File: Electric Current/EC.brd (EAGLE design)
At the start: 61.3 x 30.5 mm, 24 parts, among them IC1 LD117AS33TR

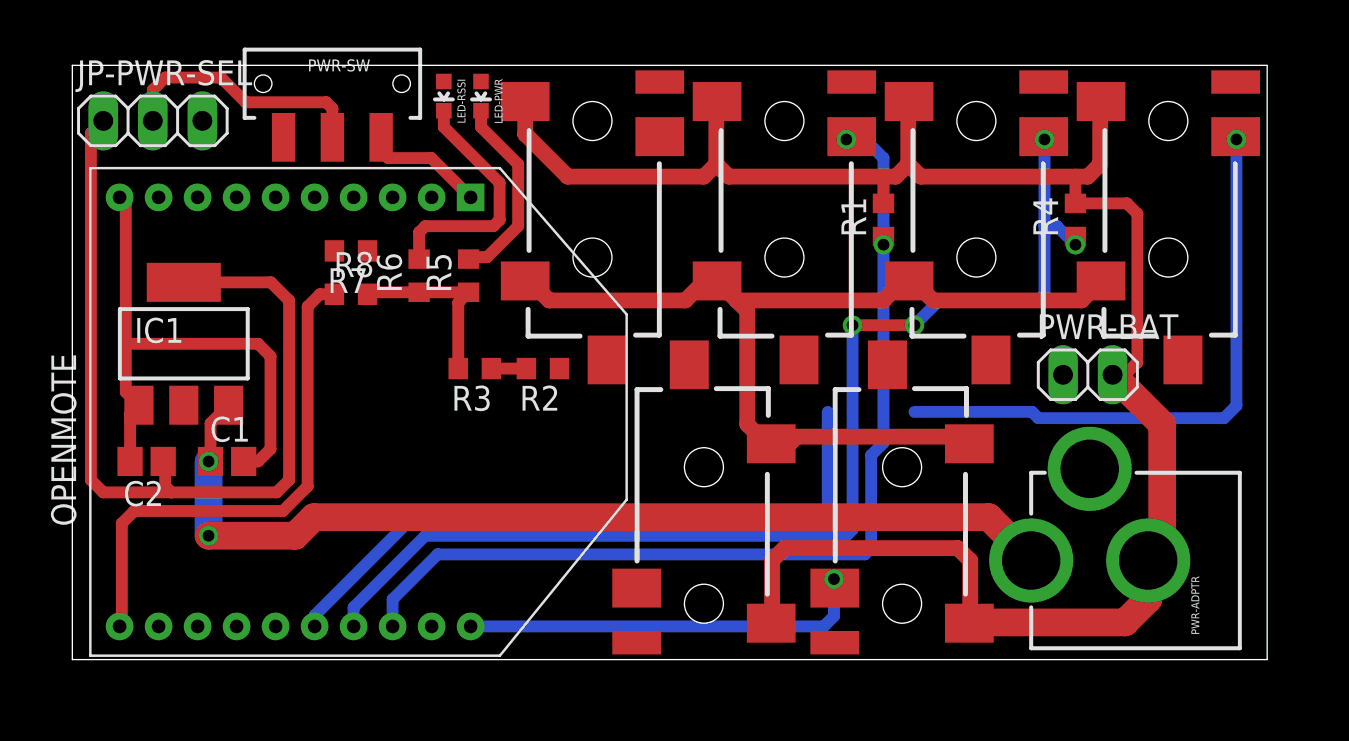
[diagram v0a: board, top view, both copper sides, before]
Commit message: Electric current module
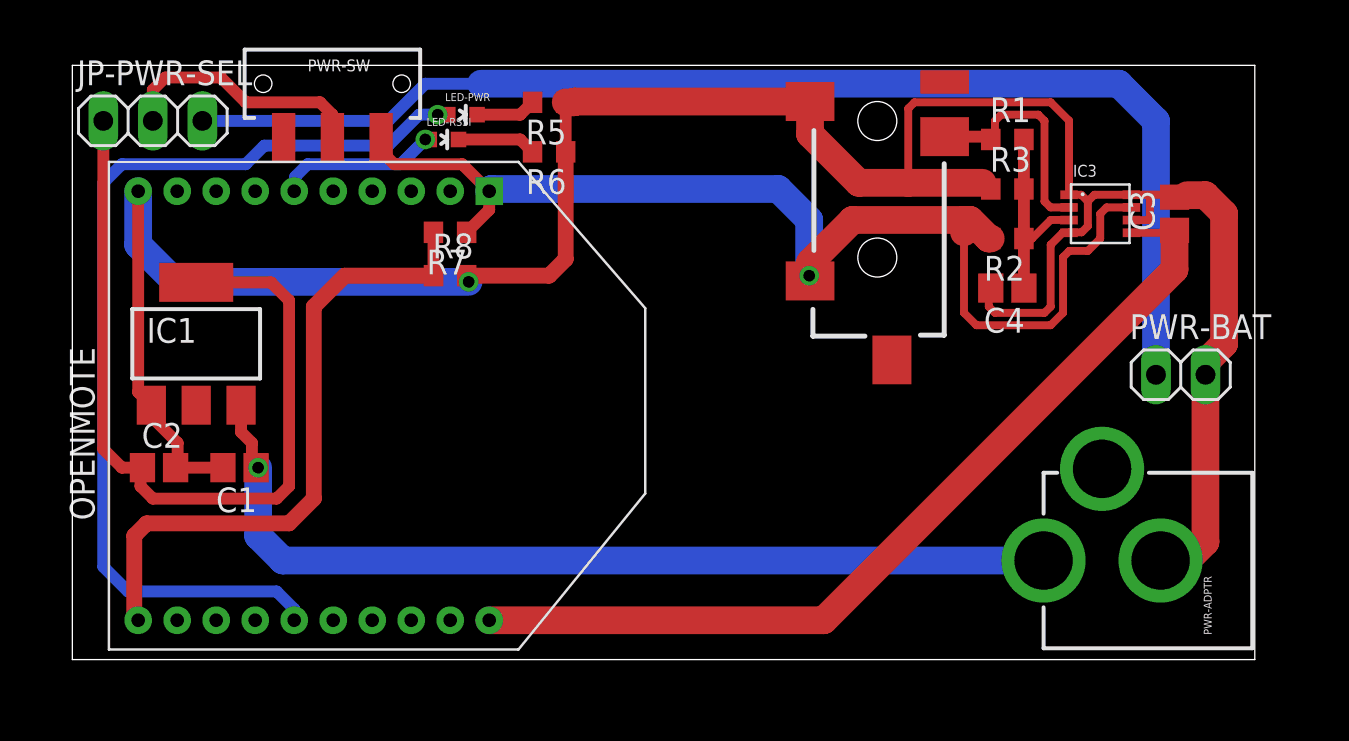
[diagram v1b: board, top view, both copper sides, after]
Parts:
- removed R4: 60R, resistor:R0603
- removed U1, U2, U4, U5, U6: (no value), SparkFun-Connectors:AUDIO-JACK-3.5MM-SMD
- added C3, C4: 1uF, resistor:C0805
- added IC3: LTC-1966MSOP-8, custom-tigor:MSOP-8
- R1: value 120R -> 50R
- R2: value 2K -> 100K
- R3: value 1K -> 100K
- moved R3 28.8 mm to (47.9, 24.1), turned to 0 degrees
- moved R2 24.7 mm to (47.9, 21.6)
- moved R5 9.80 mm to (24.4, 28.6), turned to 180 degrees
- moved R6 9.21 mm to (24.4, 26.0), turned to 180 degrees
- moved R1 7.57 mm to (47.9, 26.7), turned to 0 degrees
- moved R7 5.17 mm to (19.4, 21.9)
- moved R8 5.17 mm to (19.4, 19.7)
- moved PWR-BAT 4.76 mm to (56.8, 14.6)
- moved U3 4.76 mm to (41.3, 31.1)
- moved LED-RSSI 2.22 mm to (19.1, 26.7), turned to 270 degrees
- moved LED-PWR 1.35 mm to (20.0, 27.9), turned to 270 degrees
- moved OPENMOTE 1.00 mm to (15.9, 13.0)
- moved C2 0.71 mm to (4.45, 9.84), turned to 0 degrees
- moved C1 0.71 mm to (8.57, 9.84), turned to 180 degrees
- moved IC1 0.63 mm to (6.35, 16.2)
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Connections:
- removed net 0-10V: R2.1, U4.RING
- removed net AN-IN-0-10V-1: OPENMOTE.19, R2.2, R3.1
- removed net AN-IN-0-50MA-1: OPENMOTE.17, R4.1, U5.RING
- removed net AN-IN-3.3V-1: OPENMOTE.20, U1.RING
- removed net AN-IN-4-20MA-1: OPENMOTE.18, R1.1, U3.RING
- removed net DIG-IO-1: OPENMOTE.16, U2.RING
- removed net PWM-1: OPENMOTE.7, U6.RING
- new net AN-IN-CUR: C3.1, IC3.P$5, OPENMOTE.20
- new net CUR-SNSR: IC3.P$2, R1.1, U3.RING
- new net N$3: C4.1, IC3.P$3, R1.2, R2.1, R3.2
- net 3.3V: now also IC3.P$7, R2.2; no longer U1.TIP, U2.TIP, U4.TIP, U5.TIP, U6.TIP
- net GND: now also C3.2, C4.2, IC3.P$1, IC3.P$4, IC3.P$6, IC3.P$8, R3.1; no longer R1.2, R3.2, R4.2, U1.SLEEVE, U2.SLEEVE, U4.SLEEVE, U5.SLEEVE, U6.SLEEVE
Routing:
- net DIG-IO-1: track 64.9 -> 0.00 mm, vias 1 -> 0
- net V-BAT: track 0.00 -> 63.5 mm
- net AN-IN-0-50MA-1: track 59.7 -> 0.00 mm, vias 4 -> 0
- net ASC: track 0.00 -> 50.1 mm, vias 0 -> 1
- net AN-IN-4-20MA-1: track 50.0 -> 0.00 mm, vias 2 -> 0
- net AN-IN-CUR: track 0.00 -> 46.8 mm
- net AN-IN-3.3V-1: track 21.2 -> 0.00 mm, vias 1 -> 0
- net CUR-SNSR: track 0.00 -> 11.8 mm
- net N$3: track 0.00 -> 10.3 mm
- net N$2: track 12.5 -> 4.06 mm
- net RSSI: track 0.00 -> 8.43 mm, vias 0 -> 1
- net N$1: track 9.95 -> 3.11 mm
- net AN-IN-VCC: track 26.5 -> 33.3 mm
- net 3.3V: track 56.3 -> 59.8 mm, vias 0 -> 1
- net V-ADPTR: track 46.1 -> 43.0 mm
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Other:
- board size 61.3 x 30.5 mm -> 60.6 x 30.5 mm

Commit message: 3 phase meter, add spacer, reset LTC 1966 dim
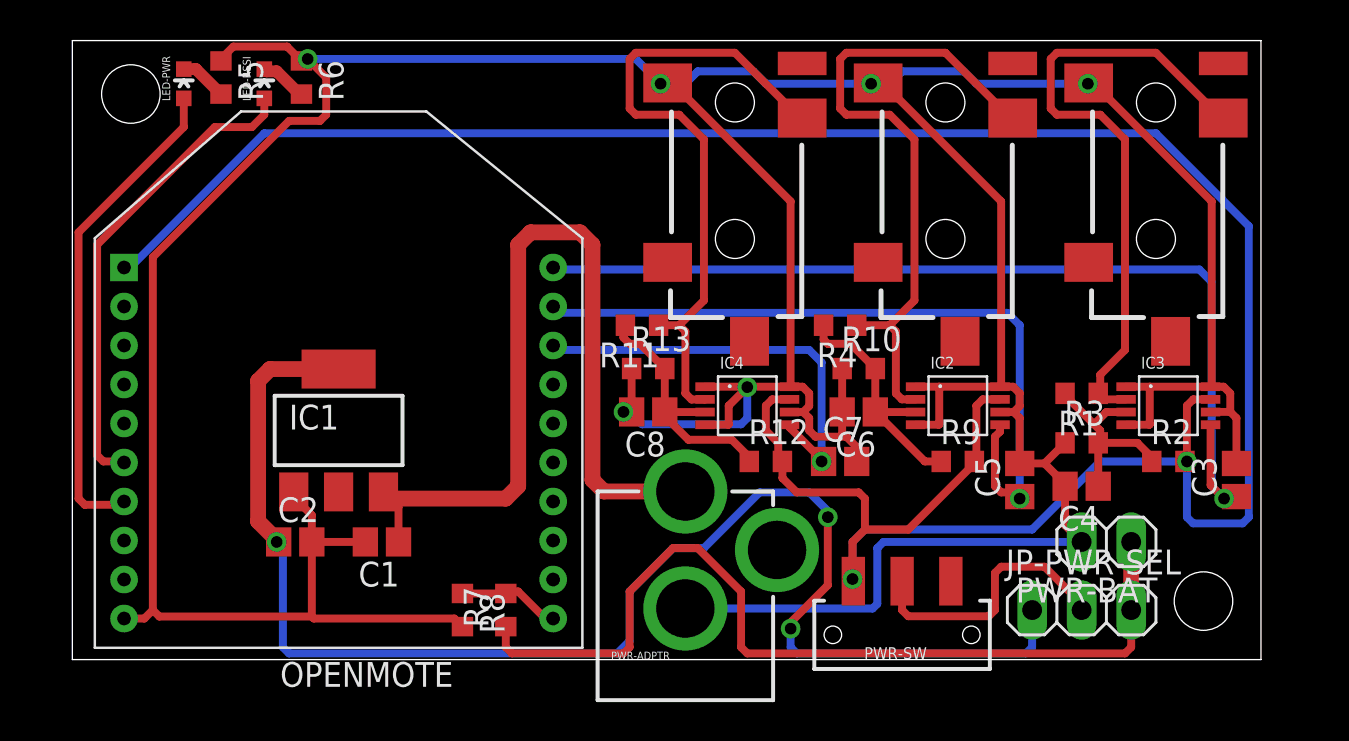
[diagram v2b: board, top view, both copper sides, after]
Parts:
- added C5, C6, C7, C8: 1uF, resistor:C0805
- added IC2, IC4: LTC-1966MSOP-8, custom-tigor:MSOP-8
- added R10, R12, R13, R9: 100K, resistor:R0603
- added R11, R4: 50R, resistor:R0603
- added U1, U2: (no value), SparkFun-Connectors:AUDIO-JACK-3.5MM-SMD
- moved JP-PWR-SEL 53.8 mm to (51.8, 2.54)
- moved PWR-SW 40.6 mm to (42.5, 1.27), turned to 180 degrees
- moved PWR-ADPTR 33.6 mm to (31.4, -5.08), turned to 0 degrees
- moved R7 19.6 mm to (22.2, 2.54), turned to 90 degrees
- moved R8 17.2 mm to (20.0, 2.54), turned to 270 degrees
- moved R5 16.9 mm to (7.62, 29.8), turned to 270 degrees
- moved LED-PWR 14.4 mm to (5.71, 29.5), turned to 0 degrees
- moved U3 14.3 mm to (55.6, 32.1)
- moved R2 14.1 mm to (56.2, 10.2), turned to 0 degrees
- moved C3 14.0 mm to (59.7, 9.21)
- moved R1 13.6 mm to (51.8, 13.7), turned to 180 degrees
- moved R3 13.6 mm to (51.8, 11.1)
- moved R6 13.3 mm to (11.7, 29.8), turned to 270 degrees
- moved C4 10.9 mm to (51.8, 8.89)
- moved IC3 10.4 mm to (56.2, 13.0)
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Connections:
- net AN-IN-CUR renamed AN-IN-CUR-1
- net CUR-SNSR renamed CUR-SNSR-1
- removed net ASC: LED-PWR.A, OPENMOTE.15
- new net AN-IN-CUR-2: C5.1, IC2.P$5, OPENMOTE.19
- new net AN-IN-CUR-3: C7.1, IC4.P$5, OPENMOTE.18
- new net CUR-SNSR-2: IC2.P$2, R4.1, U1.RING
- new net CUR-SNSR-3: IC4.P$2, R11.1, U2.RING
- new net N$4: C6.1, IC2.P$3, R10.2, R4.2, R9.1
- new net N$5: C8.1, IC4.P$3, R11.2, R12.1, R13.2
- new net V-BAT-INDC: LED-PWR.A, OPENMOTE.7
- net 3.3V: now also IC2.P$7, IC4.P$7, R12.2, R9.2; no longer R7.1, U3.TIP
- net GND: now also C5.2, C6.2, C7.2, C8.2, IC2.P$1, IC2.P$4, IC2.P$6, IC2.P$8, IC4.P$1, IC4.P$4, IC4.P$6, IC4.P$8, R10.1, R13.1, U1.SLEEVE, U2.SLEEVE
- net V-BAT: now also R7.1
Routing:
- net GND: track 134.9 -> 250.6 mm, vias 1 -> 6
- net 3.3V: track 59.8 -> 134.7 mm, vias 1 -> 2
- net ASC: track 50.1 -> 0.00 mm, vias 1 -> 0
- net AN-IN-CUR-2: track 0.00 -> 38.0 mm, vias 0 -> 1
- net CUR-SNSR-2: track 0.00 -> 33.9 mm
- net CUR-SNSR-3: track 0.00 -> 33.2 mm
- net V-ADPTR: track 43.0 -> 74.3 mm, vias 0 -> 3
- net AN-IN-VCC: track 33.3 -> 5.27 mm
- net V-BAT-INDC: track 0.00 -> 25.3 mm
- net AN-IN-CUR-3: track 0.00 -> 21.8 mm, vias 0 -> 1
- net CUR-SNSR-1: track 11.8 -> 32.5 mm
- net V-BAT: track 63.5 -> 46.6 mm
- net RSSI: track 8.43 -> 24.5 mm, vias 1 -> 0
- net N$5: track 0.00 -> 13.4 mm
- net N$4: track 0.00 -> 12.7 mm
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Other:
- board size 60.6 x 30.5 mm -> 60.9 x 31.7 mm
